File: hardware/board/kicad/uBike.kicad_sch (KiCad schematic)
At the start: 29 parts, among them J1 KMDGX-6S-BS, J2 F31S-1A7L1-11040, J3 KMDGX-8S-BS, J4 FTSH-105-01-F-DV-K, Q1 MMBT3904, U1 SN65HVD08DR, U2 LD1117S33TR_SOT223, U3 MDBT50Q-P1MV2, X1 32.768kHz

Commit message: Roughed in
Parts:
- removed C1, C2: 100nF, Capacitor_SMD:C_0805_2012Metric, symbol Device:C
- removed C3: 10uF, Capacitor_SMD:C_1206_3216Metric, symbol Device:C
- removed J1: KMDGX-6S-BS, libs:KMDGX6SBS, symbol KMDGX-6S-BS:KMDGX-6S-BS
- removed J3: KMDGX-8S-BS, libs:KMDGX8SBS, symbol KMDGX-8S-BS:KMDGX-8S-BS
- removed J4: FTSH-105-01-F-DV-K, libs:FTSH10501FDVK, symbol FTSH-105-01-F-DV-K:FTSH-105-01-F-DV-K
- removed R4: 10k, Resistor_SMD:R_0603_1608Metric, symbol Device:R
- removed R5: 120, Resistor_SMD:R_0603_1608Metric, symbol Device:R
- removed U1: SN65HVD08DR, libs:SOIC127P600X175-8N, symbol SN65HVD08DR:SN65HVD08DR
- removed U2: LD1117S33TR_SOT223, Package_TO_SOT_SMD:SOT-223-3_TabPin2, symbol Regulator_Linear:LD1117S33TR_SOT223
- added D2: GREEN, Diode_SMD:D_1206_3216Metric, symbol Device:LED
- added H4: MountingHole, MountingHole:MountingHole_3.2mm_M3, symbol Mechanical:MountingHole
- added R20: 68, Resistor_SMD:R_0805_2012Metric, symbol Device:R
- H1, H2, H3: footprint MountingHole:MountingHole_2.7mm_M2.5 -> MountingHole:MountingHole_3.2mm_M3
- R1, R2, R3, R6, R7, R8: value 390 -> 68
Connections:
- net GND: now also R20.1
- net at U3.37 (P0.13): now also D2.2 (A)
- net SWDIO: now reaches U3.51 (SWDIO)
- net SWCLK: now reaches U3.53 (SWDCLK)
- net +12V renamed +5V
- net XL renamed CTP_SCL
- net XR renamed CTP_SDA
- new net: D2.1 (K), R20.2
- no-connect marks 44 -> 33
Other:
- added sheet External Connections (external-connections.kicad_sch)
- moved on the sheet: C4, C5, C6, J2, Q1, R1, R10, R11, R2, R3, R6, R7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

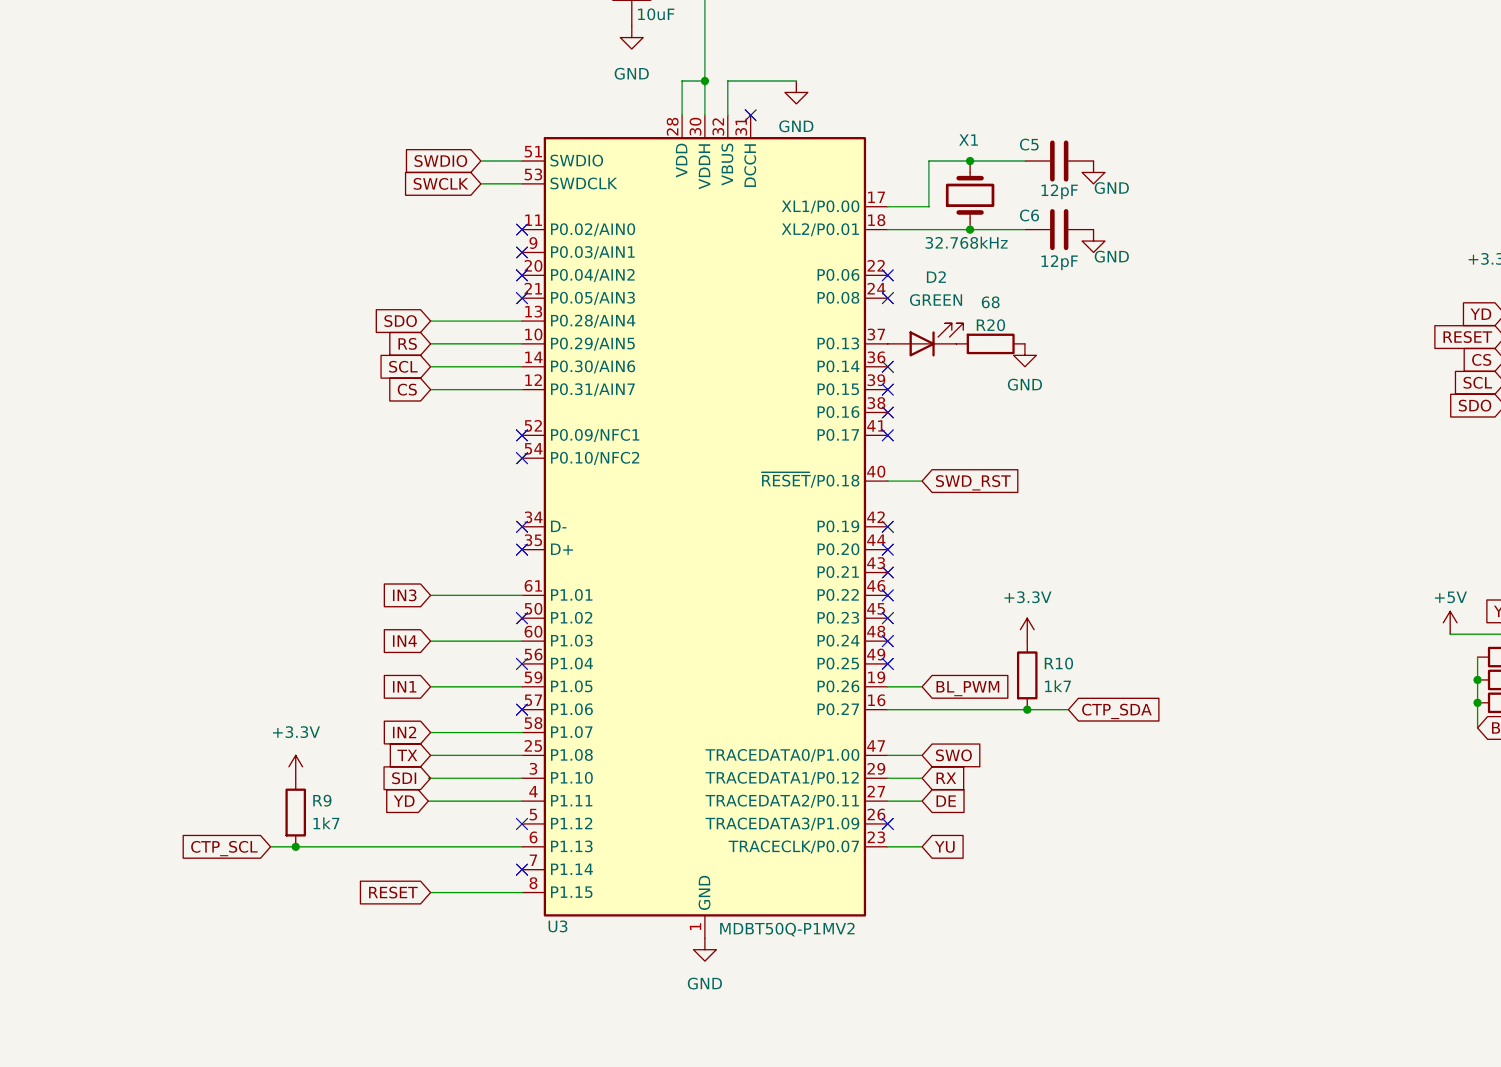
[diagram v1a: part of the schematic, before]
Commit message: Changed to 2-layer board
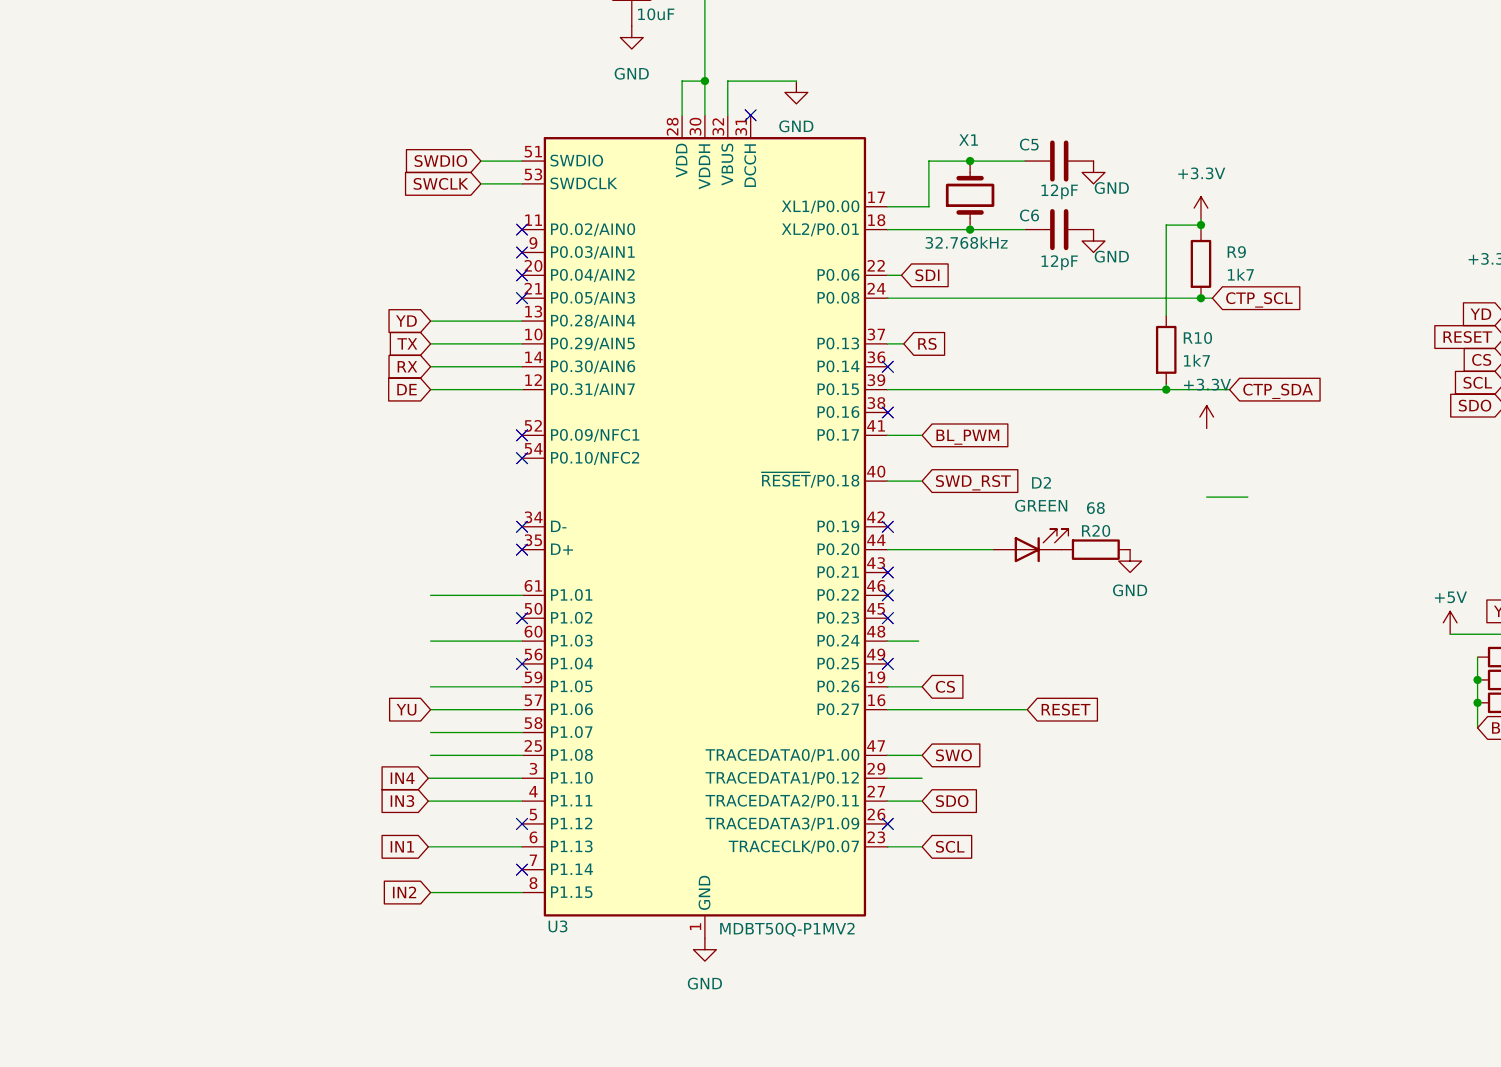
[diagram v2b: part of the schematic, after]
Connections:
- net BL_PWM: now also U3.41 (P0.17); no longer U3.19 (P0.26)
- net CS: now also U3.19 (P0.26); no longer U3.12 (P0.31/AIN7)
- net CTP_SCL: now also U3.24 (P0.08); no longer U3.6 (P1.13)
- net CTP_SDA: now also U3.39 (P0.15); no longer U3.16 (P0.27)
- net DE: now also U3.12 (P0.31/AIN7); no longer U3.27 (TRACEDATA2/P0.11)
- net IN1: now also U3.6 (P1.13); no longer U3.59 (P1.05)
- net IN2: now also U3.8 (P1.15); no longer U3.58 (P1.07)
- net IN3: now also U3.4 (P1.11); no longer U3.61 (P1.01)
- net IN4: now also U3.3 (P1.10); no longer U3.60 (P1.03)
- net RESET: now also U3.16 (P0.27); no longer U3.8 (P1.15)
- net RS: now also U3.37 (P0.13); no longer U3.10 (P0.29/AIN5)
- net RX: now also U3.14 (P0.30/AIN6); no longer U3.29 (TRACEDATA1/P0.12)
- net SCL: now also U3.23 (TRACECLK/P0.07); no longer U3.14 (P0.30/AIN6)
- net SDI: now also U3.22 (P0.06); no longer U3.3 (P1.10)
- net SDO: now also U3.27 (TRACEDATA2/P0.11); no longer U3.13 (P0.28/AIN4)
- net TX: now also U3.10 (P0.29/AIN5); no longer U3.25 (P1.08)
- net YD: now also U3.13 (P0.28/AIN4); no longer U3.4 (P1.11)
- net YU: now also U3.57 (P1.06); no longer U3.23 (TRACECLK/P0.07)
- net at D2.2 (A): now also U3.44 (P0.20); no longer U3.37 (P0.13)
- no-connect marks 33 -> 26
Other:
- moved on the sheet: D2, R10, R20, R9

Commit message: Schematic cleanup
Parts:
- added J4: TC2050-IDC-NL, Connector:Tag-Connect_TC2050-IDC-NL_2x05_P1.27mm_Vertical, symbol TC2050-IDC-NL:TC2050-IDC-NL
- C4: value 10uF -> 10u
- C5, C6: value 12pF -> 12p
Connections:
- net +3.3V: now also J4.1
- net GND: now also J4.3, J4.5
- net IN4: now also U3.5 (P1.12); no longer U3.3 (P1.10)
- net SWCLK: now also J4.4
- net SWDIO: now also J4.2
- net SWD_RST: now also J4.10
- net SWO: now also J4.6
- no-connect marks 26 -> 36
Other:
- note added: "Raytac MDBT50A (Microcontroller)"
- note added: "Touchscreen"
- moved on the sheet: C4, C5, C6, D2, H1, H2, H3, H4, J2, Q1, R1, R10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

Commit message: Finalized for review
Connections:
- net YU: now also U3.36 (P0.14); no longer U3.57 (P1.06)
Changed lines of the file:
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@@
   (no_connect (at 62.357 73.406))
   (no_connect (at 62.357 114.046))
-  (no_connect (at 102.997 88.646))
+  (no_connect (at 62.357 126.746))
   (no_connect (at 62.357 121.666))
   (no_connect (at 62.357 116.586))
@@
     (stroke (width 0) (type default))
   )
-  (wire (pts (xy 51.943 126.746) (xy 62.357 126.746))
+  (wire (pts (xy 113.411 88.646) (xy 102.997 88.646))
     (stroke (width 0) (type default))
   )
@@
     )
   )
-  (global_label "YU" (shape input) (at 51.943 126.746 180) (fields_autoplaced)
-    (effects (font (size 1.27 1.27)) (justify right))
-    (property "Intersheetrefs" "${INTERSHEET_REFS}" (at 46.5387 126.746 0)
-      (effects (font (size 1.27 1.27)) (justify right) hide)
-    )
-  )
+  (global_label "YU" (shape input) (at 113.411 88.646 0) (fields_autoplaced)
+    (effects (font (size 1.27 1.27)) (justify left))
+    (property "Intersheetrefs" "${INTERSHEET_REFS}" (at 118.8153 88.646 0)
+      (effects (font (size 1.27 1.27)) (justify left) hide)
+    )
+  )

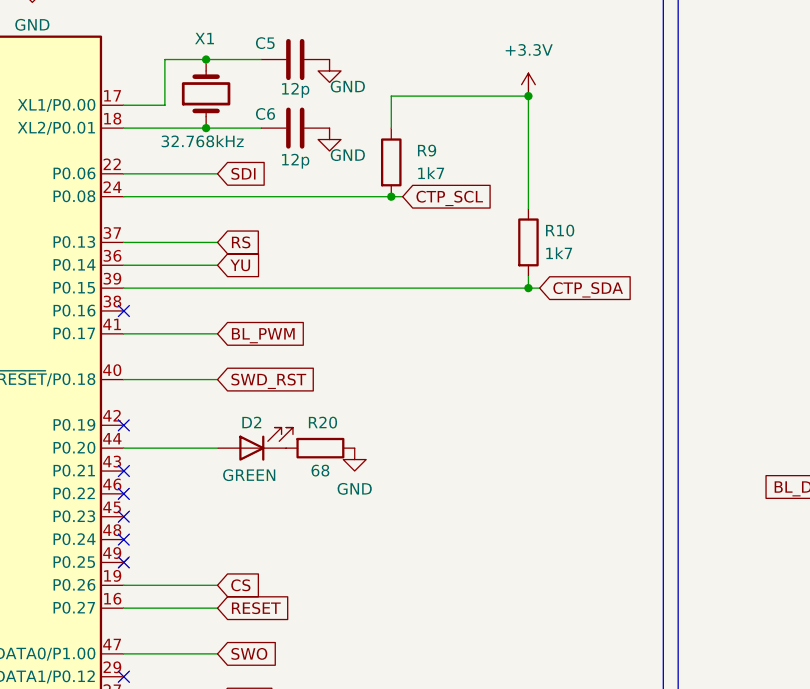
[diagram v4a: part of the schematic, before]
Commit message: Changed 2.2uF cap footprints and a bit more cleanup
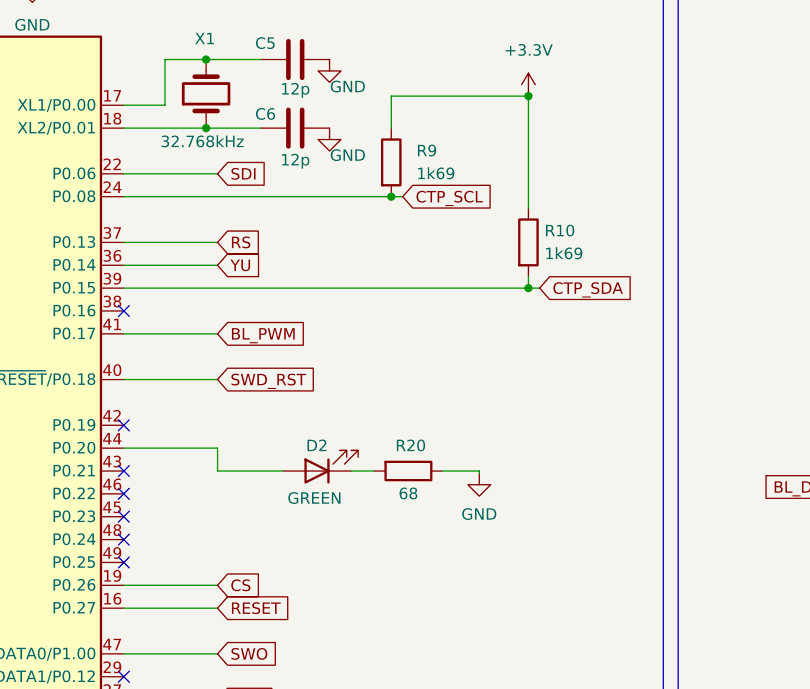
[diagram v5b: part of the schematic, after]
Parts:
- C4: Manufacturer_Name (none) -> Murata Electronics; Manufacturer_Part_Number (none) -> GRM319R61E106MA12D; Mouser Part Number (none) -> 81-GRM319R61E106MA2D
- C5, C6: Manufacturer_Name (none) -> Kemet; Manufacturer_Part_Number (none) -> C0603C120F5GACTU; Mouser Part Number (none) -> 80-C0603C120F5G
- D2: Manufacturer_Name (none) -> Lite-On; Manufacturer_Part_Number (none) -> LTST-C150KGKT; Mouser Part Number (none) -> 859-LTST-C150KGKT
- H1, H2, H3, H4, J4: Manufacturer_Name (none) -> -; Manufacturer_Part_Number (none) -> -
- J2: Manufacturer_Name AMPHENOL COMMUNICATION SOLUTIONS -> Amphenol ICC; Mouser Part Number (none) -> 649-F31S-1A7L1-11040
- Q1: Manufacturer_Name (none) -> Diotec Semiconductor; Manufacturer_Part_Number (none) -> MMBT3904; Mouser Part Number (none) -> 637-MMBT3904
- R1, R2, R20, R3, R6, R7, R8: Manufacturer_Name (none) -> Panasonic; Manufacturer_Part_Number (none) -> ERJ-P06F68R0V; Mouser Part Number (none) -> 667-ERJ-P06F68R0V
- R10, R9: value 1k7 -> 1k69; Manufacturer_Name (none) -> Panasonic; Manufacturer_Part_Number (none) -> ERJ-PA3F1691V; Mouser Part Number (none) -> 667-ERJ-PA3F1691V
- R11: Manufacturer_Name (none) -> Panasonic; Manufacturer_Part_Number (none) -> ERJ-PA3F1001V; Mouser Part Number (none) -> 667-ERJ-PA3F1001V
- U3: Manufacturer_Name (none) -> Raytac Corporation; Manufacturer_Part_Number (none) -> MDBT50Q-1MV2; Mouser Part Number (none) -> 485-4078
- X1: Manufacturer_Name (none) -> NDK; Manufacturer_Part_Number (none) -> NX3215SA-32.768K-STD-MUA-9; Mouser Part Number (none) -> 344-NX3215SA32768K9
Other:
- moved on the sheet: D2, R20
